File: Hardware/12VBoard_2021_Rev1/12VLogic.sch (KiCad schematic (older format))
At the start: 7 parts

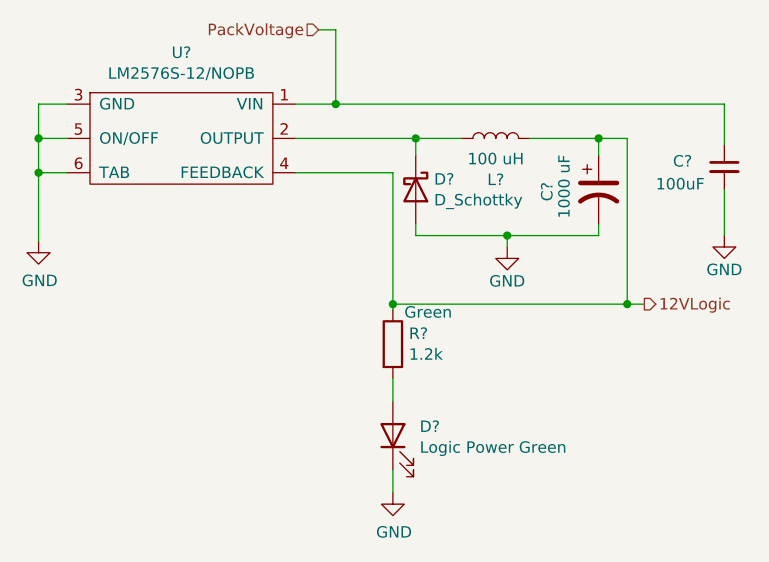
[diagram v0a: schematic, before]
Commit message: Redesigned low current ports schematic
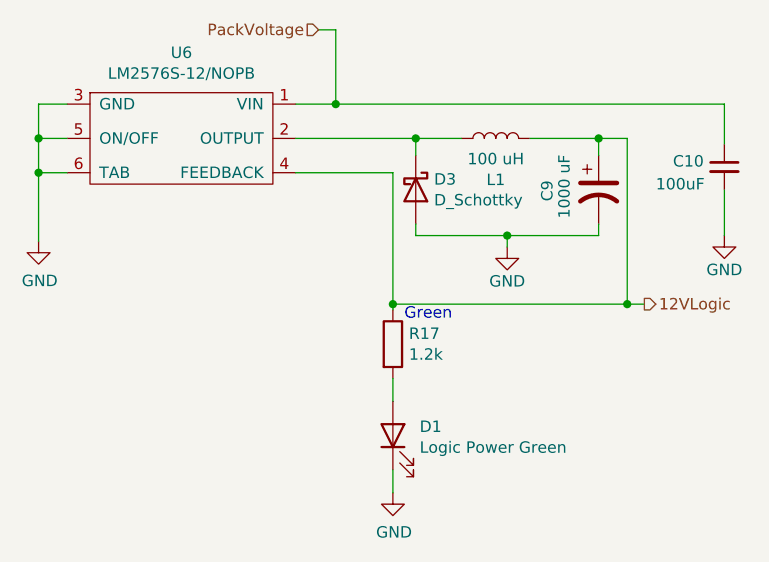
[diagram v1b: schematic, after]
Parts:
- gave numbers to parts that had none: 7
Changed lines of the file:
@@
 AR Path="/5F74F36B/5F8236F9/5FB8C58F" Ref="C?"  Part="1"
 AR Path="/5F74F36B/5FB8C58F" Ref="C?"  Part="1"
-AR Path="/5F74F36B/5FB68F3E/5FB8C58F" Ref="C?"  Part="1"
-F 0 "C?" H 7200 3300 50  0000 L CNN
+AR Path="/5F74F36B/5FB68F3E/5FB8C58F" Ref="C10"  Part="1"
+F 0 "C10" H 7200 3300 50  0000 L CNN
 F 1 "100uF" H 7125 3200 50  0000 L CNN
 F 2 "Capacitor_SMD:C_0603_1608Metric_Pad1.05x0.95mm_HandSolder" H 7425 3275 50  0001 C CNN
@@
 AR Path="/5F74F36B/5F8236F9/5FB8C595" Ref="D?"  Part="1"
 AR Path="/5F74F36B/5FB8C595" Ref="D?"  Part="1"
-AR Path="/5F74F36B/5FB68F3E/5FB8C595" Ref="D?"  Part="1"
-F 0 "D?" V 6029 3455 50  0000 L CNN
+AR Path="/5F74F36B/5FB68F3E/5FB8C595" Ref="D3"  Part="1"
+F 0 "D3" V 6029 3455 50  0000 L CNN
 F 1 "D_Schottky" V 6120 3455 50  0000 L CNN
 F 2 "Diode_THT:D_DO-201AD_P5.08mm_Vertical_KathodeUp" H 6075 3375 50  0001 C CNN
@@
 AR Path="/5F74F36B/5F8236F9/5FB8C5B2" Ref="#PWR?"  Part="1"
 AR Path="/5F74F36B/5FB8C5B2" Ref="#PWR?"  Part="1"
-AR Path="/5F74F36B/5FB68F3E/5FB8C5B2" Ref="#PWR?"  Part="1"
-F 0 "#PWR?" H 4425 3350 50  0001 C CNN
+AR Path="/5F74F36B/5FB68F3E/5FB8C5B2" Ref="#PWR06"  Part="1"
+F 0 "#PWR06" H 4425 3350 50  0001 C CNN
 F 1 "GND" H 4430 3427 50  0000 C CNN
 F 2 "" H 4425 3600 50  0001 C CNN
@@
 AR Path="/5F74F36B/5F8236F9/5FB8C5C1" Ref="U?"  Part="1"
 AR Path="/5F74F36B/5FB8C5C1" Ref="U?"  Part="1"
-AR Path="/5F74F36B/5FB68F3E/5FB8C5C1" Ref="U?"  Part="1"
-F 0 "U?" H 5050 3625 50  0000 C CNN
+AR Path="/5F74F36B/5FB68F3E/5FB8C5C1" Ref="U6"  Part="1"
+F 0 "U6" H 5050 3625 50  0000 C CNN
 F 1 "LM2576S-12/NOPB" H 5050 3534 50  0000 C CNN
 F 2 "MRDT_Devices:LM2576" H 5050 3650 50  0001 C CNN
@@
 AR Path="/5F74F36B/5F8236F9/5FB8C5C7" Ref="#PWR?"  Part="1"
 AR Path="/5F74F36B/5FB8C5C7" Ref="#PWR?"  Part="1"
-AR Path="/5F74F36B/5FB68F3E/5FB8C5C7" Ref="#PWR?"  Part="1"
-F 0 "#PWR?" H 6475 3375 50  0001 C CNN
+AR Path="/5F74F36B/5FB68F3E/5FB8C5C7" Ref="#PWR09"  Part="1"
+F 0 "#PWR09" H 6475 3375 50  0001 C CNN
 F 1 "GND" H 6475 3475 50  0000 C CNN
 F 2 "" H 6475 3625 50  0001 C CNN
@@
 AR Path="/5F74F36B/5F8236F9/5FB8C5CD" Ref="C?"  Part="1"
 AR Path="/5F74F36B/5FB8C5CD" Ref="C?"  Part="1"
-AR Path="/5F74F36B/5FB68F3E/5FB8C5CD" Ref="C?"  Part="1"
-F 0 "C?" V 6650 3325 50  0000 L CNN
+AR Path="/5F74F36B/5FB68F3E/5FB8C5CD" Ref="C9"  Part="1"
+F 0 "C9" V 6650 3325 50  0000 L CNN
 F 1 "1000 uF" V 6725 3250 50  0000 L CNN
 F 2 "Capacitor_THT:CP_Radial_D10.0mm_P5.00mm" H 6875 3375 50  0001 C CNN
@@
 AR Path="/5F74F36B/5F8236F9/5FB8C5D3" Ref="L?"  Part="1"
 AR Path="/5F74F36B/5FB8C5D3" Ref="L?"  Part="1"
-AR Path="/5F74F36B/5FB68F3E/5FB8C5D3" Ref="L?"  Part="1"
-F 0 "L?" V 6244 3150 50  0000 C CNN
+AR Path="/5F74F36B/5FB68F3E/5FB8C5D3" Ref="L1"  Part="1"
+F 0 "L1" V 6244 3150 50  0000 C CNN
 F 1 "100 uH" V 6335 3150 50  0000 C CNN
 F 2 "Inductor_SMD:L_0603_1608Metric_Pad1.05x0.95mm_HandSolder" H 6425 3150 50  0001 C CNN
@@
 AR Path="/5F74F36B/5F8236F9/5FB8C5D9" Ref="#PWR?"  Part="1"
 AR Path="/5F74F36B/5FB8C5D9" Ref="#PWR?"  Part="1"
-AR Path="/5F74F36B/5FB68F3E/5FB8C5D9" Ref="#PWR?"  Part="1"
-F 0 "#PWR?" H 7425 3325 50  0001 C CNN
+AR Path="/5F74F36B/5FB68F3E/5FB8C5D9" Ref="#PWR010"  Part="1"
+F 0 "#PWR010" H 7425 3325 50  0001 C CNN
 F 1 "GND" H 7425 3425 50  0000 C CNN
 F 2 "" H 7425 3575 50  0001 C CNN
@@
 AR Path="/5F74F36B/5F8236F9/5FB8C5E4" Ref="R?"  Part="1"
 AR Path="/5F74F36B/5FB8C5E4" Ref="R?"  Part="1"
-AR Path="/5F74F36B/5FB68F3E/5FB8C5E4" Ref="R?"  Part="1"
-F 0 "R?" H 6045 4096 50  0000 L CNN
+AR Path="/5F74F36B/5FB68F3E/5FB8C5E4" Ref="R17"  Part="1"
+F 0 "R17" H 6045 4096 50  0000 L CNN
 F 1 "1.2k" H 6045 4005 50  0000 L CNN
 F 2 "Resistor_SMD:R_0603_1608Metric_Pad1.05x0.95mm_HandSolder" V 5905 4050 50  0001 C CNN
@@
 AR Path="/5F74F36B/5F8236F9/5FB8C5EA" Ref="#PWR?"  Part="1"
 AR Path="/5F74F36B/5FB8C5EA" Ref="#PWR?"  Part="1"
-AR Path="/5F74F36B/5FB68F3E/5FB8C5EA" Ref="#PWR?"  Part="1"
-F 0 "#PWR?" H 5975 4450 50  0001 C CNN
+AR Path="/5F74F36B/5FB68F3E/5FB8C5EA" Ref="#PWR08"  Part="1"
+F 0 "#PWR08" H 5975 4450 50  0001 C CNN
 F 1 "GND" H 5980 4527 50  0000 C CNN
 F 2 "" H 5975 4700 50  0001 C CNN
@@
 AR Path="/5F74F36B/5F8236F9/5FB8C5F0" Ref="D?"  Part="1"
 AR Path="/5F74F36B/5FB8C5F0" Ref="D?"  Part="1"
-AR Path="/5F74F36B/5FB68F3E/5FB8C5F0" Ref="D?"  Part="1"
-F 0 "D?" V 6014 4333 50  0000 R CNN
+AR Path="/5F74F36B/5FB68F3E/5FB8C5F0" Ref="D1"  Part="1"
+F 0 "D1" V 6014 4333 50  0000 R CNN
 F 1 "Logic Power Green" V 5923 4333 50  0000 R CNN
 F 2 "Diode_SMD:D_0603_1608Metric_Pad1.05x0.95mm_HandSolder" H 5975 4450 50  0001 C CNN

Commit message: Layed out logic power
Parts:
- C9: footprint Capacitor_THT:CP_Radial_D10.0mm_P5.00mm -> Capacitor_THT:CP_Radial_D12.5mm_P5.00mm
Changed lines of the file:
@@
 F 0 "C9" V 6650 3325 50  0000 L CNN
 F 1 "1000 uF" V 6725 3250 50  0000 L CNN
-F 2 "Capacitor_THT:CP_Radial_D10.0mm_P5.00mm" H 6875 3375 50  0001 C CNN
+F 2 "Capacitor_THT:CP_Radial_D12.5mm_P5.00mm" H 6875 3375 50  0001 C CNN
 F 3 "~" H 6875 3375 50  0001 C CNN
 	1    6875 3375

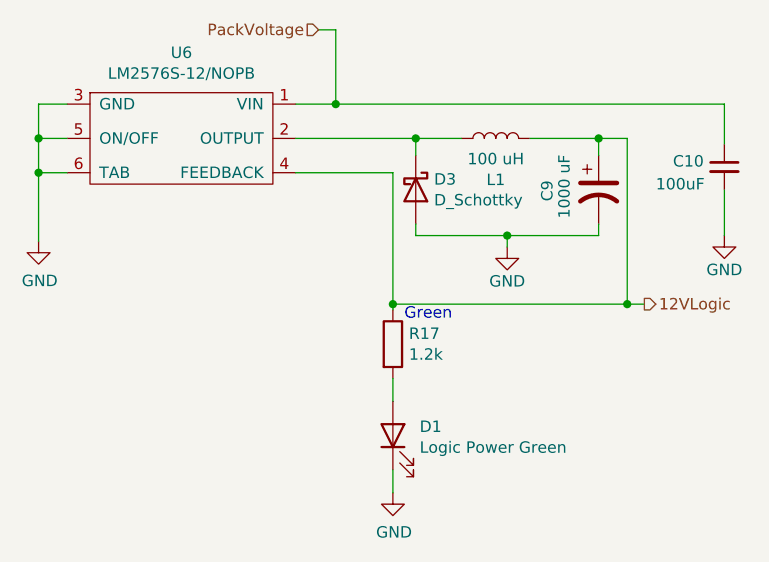
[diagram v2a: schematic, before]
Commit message: changed to big bucks
changed to the bucks used in Master due to a realization in the inductor sizing for the LM5116. It would be much bigger than previous years.
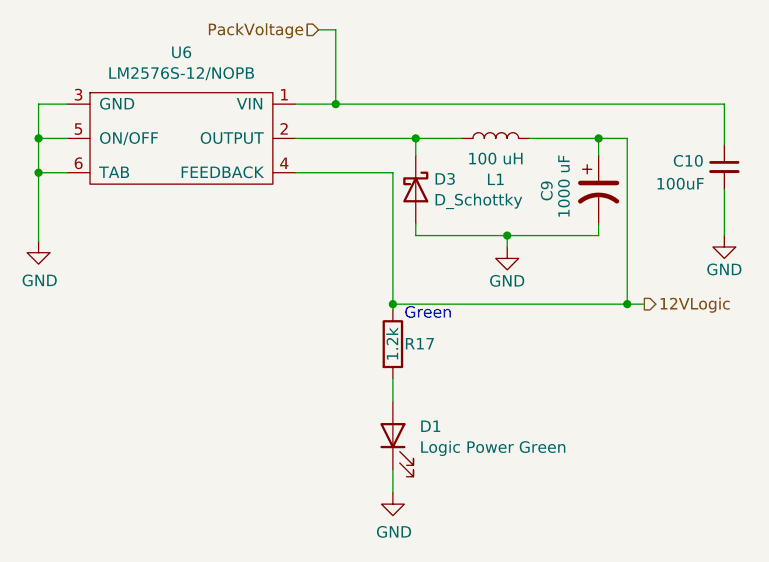
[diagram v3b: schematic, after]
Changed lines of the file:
@@
 $Descr A4 11693 8268
 encoding utf-8
-Sheet 7 9
+Sheet 6 9
 Title ""
 Date ""
@@
 AR Path="/5F74F36B/5FB8C5E4" Ref="R?"  Part="1"
 AR Path="/5F74F36B/5FB68F3E/5FB8C5E4" Ref="R17"  Part="1"
-F 0 "R17" H 6045 4096 50  0000 L CNN
-F 1 "1.2k" H 6045 4005 50  0000 L CNN
+F 0 "R17" H 6025 4050 50  0000 L CNN
+F 1 "1.2k" V 5975 3975 50  0000 L CNN
 F 2 "Resistor_SMD:R_0603_1608Metric_Pad1.05x0.95mm_HandSolder" V 5905 4050 50  0001 C CNN
 F 3 "~" H 5975 4050 50  0001 C CNN
